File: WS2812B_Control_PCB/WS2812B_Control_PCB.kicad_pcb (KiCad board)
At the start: 2 copper layers, 46.5 x 91.9 mm, 27 parts, among them J1 TB002-500-02BE, J2 TB002-500-02BE, J3 Conn_01x05, J4 S3B-XH-ALFSN, J5 S3B-XH-ALFSN, J6 S3B-XH-ALFSN, J7 S3B-XH-ALFSN, J8 S3B-XH-ALFSN, U1 IRM-20-5, U2 113991254, U3 MC74VHCT50ADTR2G

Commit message: Added 4A current limit to silkscreen
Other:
- board text added: "4A"
- board text added: "IRM-20-5 20W 5V"
- board text removed: "IRM-20-5"
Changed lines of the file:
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@@
 		)
 	)
-	(gr_text "5V"
+	(gr_text "5V\n"
 		(at 17.653 63.627 0)
 		(layer "F.SilkS")
@@
 		)
 	)
+	(gr_text "4A"
+		(at 20.701 63.627 0)
+		(layer "F.SilkS")
+		(effects
+			(font
+				(size 1.5 1.5)
+				(thickness 0.3)
+				(bold yes)
+			)
+			(justify left bottom)
+		)
+	)
 	(gr_text "VOUT"
-		(at 21.082 63.627 0)
+		(at 23.749 63.627 0)
 		(layer "F.SilkS")
 		(effects
@@
 		)
 	)
-	(gr_text "IRM-20-5"
-		(at 61.087 64.897 270)
+	(gr_text "IRM-20-5\n20W 5V"
+		(at 60.96 60.96 270)
 		(layer "B.SilkS")
 		(effects

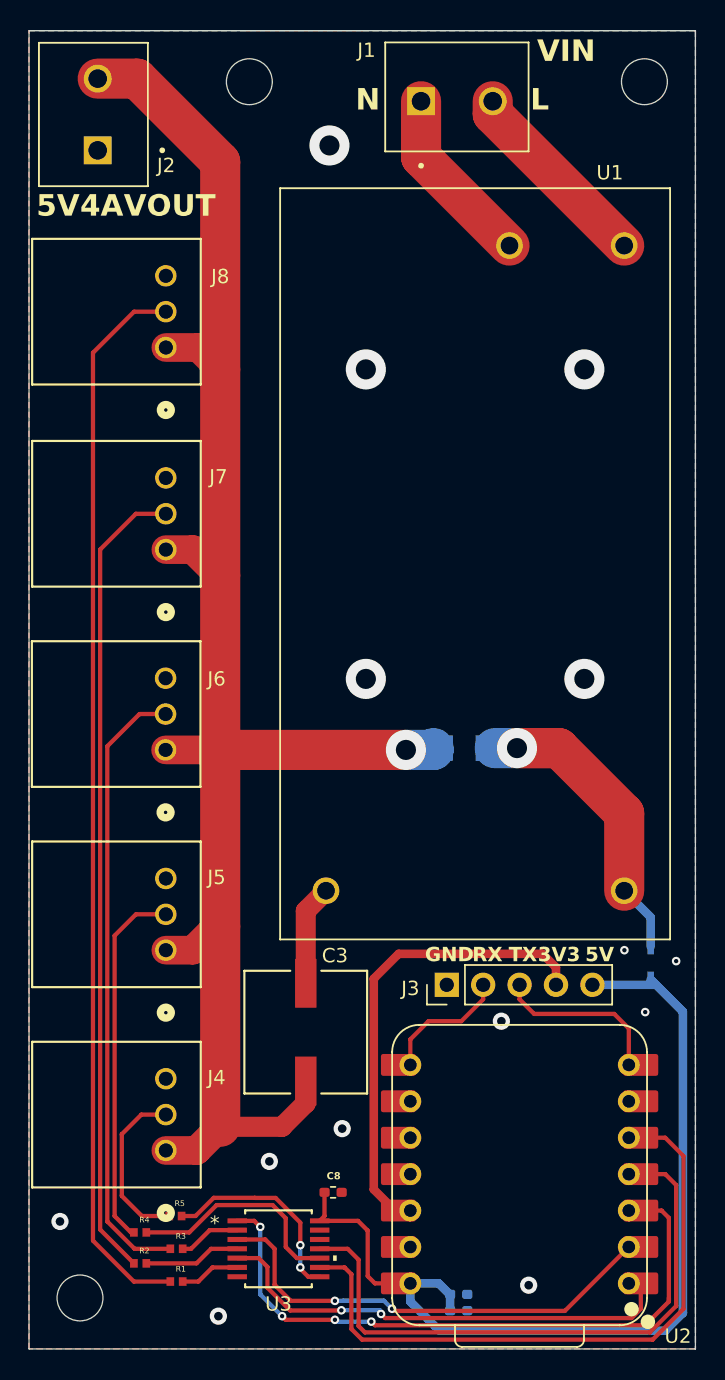
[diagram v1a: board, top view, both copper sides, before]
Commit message: Fixed flaw in v1. Pinout of IRM-20-5 was incorrect. Corrected.
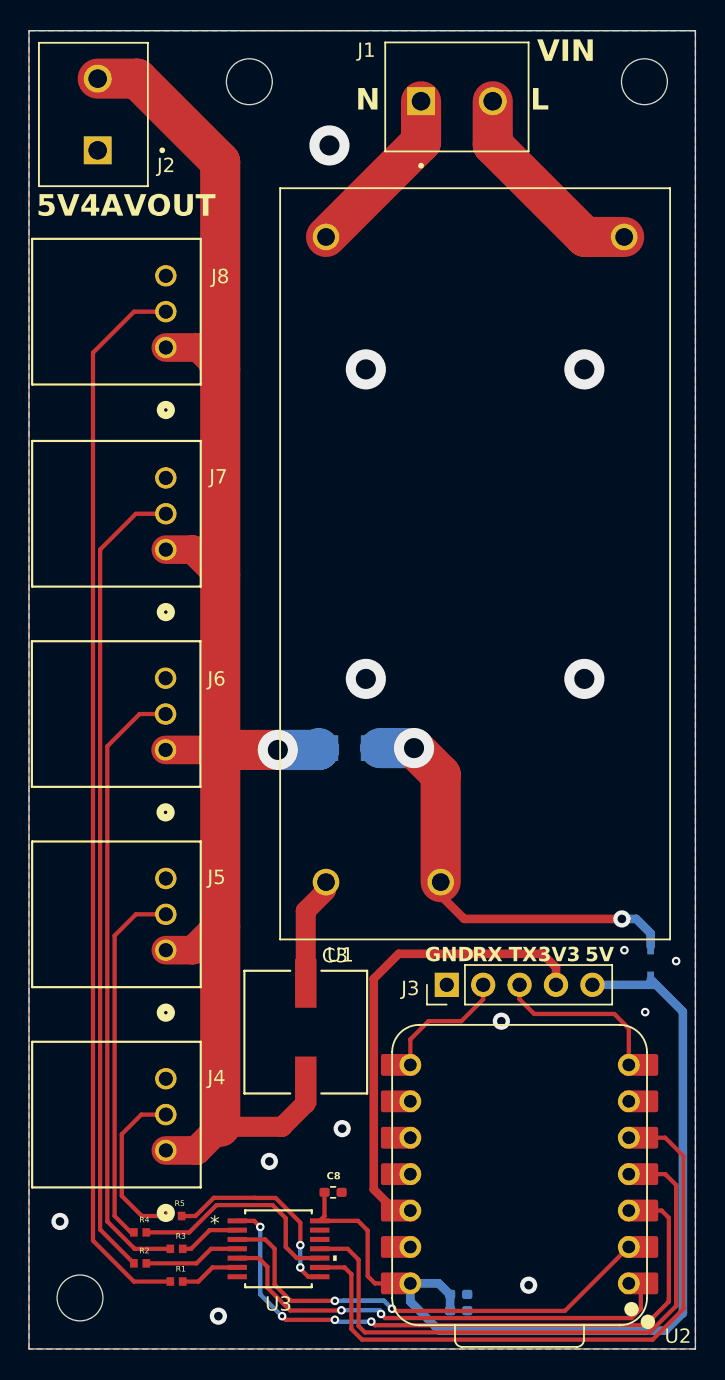
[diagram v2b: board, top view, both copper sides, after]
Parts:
- moved F1 8.00 mm to (39.5, 100.6)
- moved G*** 5.99 mm to (54.5, 106.0)
- moved G*** 1.09 mm to (51.0, 83.0)
- turned U1 to -90 degrees
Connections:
- U1 pad 1: GND -> Net-(U1-AC/L)
- U1 pad 2: VCC -> Net-(U1-AC/N)
- U1 pad 3: Net-(U1-AC/L) -> GND
- U1 pad 4: Net-(U1-AC/N) -> VCC
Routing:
- net Net-(C3-Pad1): track 123.2 -> 115.2 mm
- net VCC: track 23.3 -> 30.1 mm, vias 1 -> 2
- net Net-(U1-AC/L): track 13.9 -> 14.9 mm
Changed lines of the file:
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@@
 	(footprint "WS2812Board:CONV_IRM-20-5"
 		(layer "F.Cu")
-		(at 48.26 87.732 90)
+		(at 48.26 87.732 -90)
 		(property "Reference" "U1"
-			(at 27.28 9.398 180)
+			(at 27.28 9.398 0)
 			(layer "F.SilkS")
 			(effects
@@
 		(duplicate_pad_numbers_are_jumpers no)
 		(fp_line
-			(start 26.2 -13.6)
-			(end 26.2 13.6)
+			(start -26.2 13.6)
+			(end -26.2 -13.6)
 			(stroke
 				(width 0.127)
@@
 		)
 		(fp_line
-			(start -26.2 -13.6)
-			(end 26.2 -13.6)
+			(start 26.2 13.6)
+			(end -26.2 13.6)
 			(stroke
 				(width 0.127)
@@
 		)
 		(fp_line
-			(start 26.2 13.6)
-			(end -26.2 13.6)
+			(start -26.2 -13.6)
+			(end 26.2 -13.6)
 			(stroke
 				(width 0.127)
@@
 		)
 		(fp_line
-			(start -26.2 13.6)
-			(end -26.2 -13.6)
+			(start 26.2 -13.6)
+			(end 26.2 13.6)
 			(stroke
 				(width 0.127)
@@
 		)
 		(fp_line
-			(start 26.45 -13.85)
-			(end 26.45 13.85)
+			(start -26.45 13.85)
+			(end -26.45 -13.85)
 			(stroke
 				(width 0.05)
@@
 		)
 		(fp_line
-			(start -26.45 -13.85)
-			(end 26.45 -13.85)
+			(start 26.45 13.85)
+			(end -26.45 13.85)
 			(stroke
 				(width 0.05)
@@
 		)
 		(fp_line
-			(start 26.45 13.85)
-			(end -26.45 13.85)
+			(start -26.45 -13.85)
+			(end 26.45 -13.85)
 			(stroke
 				(width 0.05)
@@
 		)
 		(fp_line
-			(start -26.45 13.85)
-			(end -26.45 -13.85)
+			(start 26.45 -13.85)
+			(end 26.45 13.85)
 			(stroke
 				(width 0.05)
@@
 		)
 		(fp_line
-			(start 26.2 -13.6)
-			(end 26.2 13.6)
+			(start -26.2 13.6)
+			(end -26.2 -13.6)
 			(stroke
 				(width 0.127)
@@
 		)
 		(fp_line
-			(start -26.2 -13.6)
-			(end 26.2 -13.6)
+			(start 26.2 13.6)
+			(end -26.2 13.6)
 			(stroke
 				(width 0.127)
@@
 		)
 		(fp_line
-			(start 26.2 13.6)
-			(end -26.2 13.6)
+			(start -26.2 -13.6)
+			(end 26.2 -13.6)
 			(stroke
 				(width 0.127)
@@
 		)
 		(fp_line
-			(start -26.2 13.6)
-			(end -26.2 -13.6)
+			(start 26.2 -13.6)
+			(end 26.2 13.6)
 			(stroke
 				(width 0.127)
@@
 		)
 		(pad "1" thru_hole circle
-			(at -22.8 -10.4 90)
+			(at -22.8 -10.4 270)
 			(size 1.86 1.86)
 			(drill 1.24)
 			(layers "*.Cu" "*.Mask")
 			(remove_unused_layers no)
-			(net "GND")
-			(pinfunction "-V_1")
+			(net "Net-(U1-AC{slash}L)")
+			(pinfunction "AC/L_1")
 			(pintype "power_in")
 			(solder_mask_margin 0.102)
 		)
 		(pad "2" thru_hole circle
-			(at -22.8 10.4 90)
+			(at -22.8 10.4 270)
 			(size 1.86 1.86)
 			(drill 1.24)
 			(layers "*.Cu" "*.Mask")
 			(remove_unused_layers no)
-			(net "VCC")
-			(pinfunction "+V_2")
+			(net "Net-(U1-AC{slash}N)")
+			(pinfunction "AC/N_2")
 			(pintype "power_in")
 			(solder_mask_margin 0.102)
 		)
 		(pad "3" thru_hole circle
-			(at 22.2 10.4 90)
+			(at 22.2 10.4 270)
 			(size 1.86 1.86)
 			(drill 1.24)
 			(layers "*.Cu" "*.Mask")
 			(remove_unused_layers no)
-			(net "Net-(U1-AC{slash}L)")
-			(pinfunction "AC/L_3")
+			(net "GND")
+			(pinfunction "-V_3")
 			(pintype "unspecified")
 			(solder_mask_margin 0.102)
 		)
 		(pad "4" thru_hole circle
-			(at 22.2 2.4 90)
+			(at 22.2 2.4 270)
 			(size 1.86 1.86)
 			(drill 1.24)
 			(layers "*.Cu" "*.Mask")
 			(remove_unused_layers no)
-			(net "Net-(U1-AC{slash}N)")
-			(pinfunction "AC/N_4")
+			(net "VCC")
+			(pinfunction "+V_4")
 			(pintype "unspecified")
 			(solder_mask_margin 0.102)
@@
 	(footprint "WS2812Board:viiking"
 		(layer "B.Cu")
-		(at 49.53 109.347 90)
+		(at 54.5 106 90)
 		(property "Reference" "G***"
 			(at 4.572 -0.889 90)
@@
 	(footprint "WS2812Board:moomin"
 		(layer "B.Cu")
-		(at 49.911 83.058 90)
+		(at 51 83 90)
 		(property "Reference" "G***"
 			(at 0 0 90)
@@
 	(footprint "WS2812Board:C1_BEL"
 		(layer "B.Cu")
-		(at 47.498 100.584 180)
+		(at 39.5 100.584 180)
 		(tags "C1T 3.5 ")
 		(property "Reference" "F1"
@@
 			(polygon
 				(pts
-					(xy 48.2346 99.7458) (xy 46.7614 99.7458) (xy 46.7614 101.4222) (xy 48.2346 101.4222)
+					(xy 40.2366 99.7458) (xy 38.7634 99.7458) (xy 38.7634 101.4222) (xy 40.2366 101.4222)
 				)
 			)
@@
 	)
 	(segment
+		(start 34.5 100.711)
+		(end 30.48 100.711)
+		(width 2.8)
+		(layer "F.Cu")
+		(net "Net-(C3-Pad1)")
+	)
+	(segment
 		(start 30.48 113.03)
 		(end 30.48 100.711)
@@
 	)
 	(segment
-		(start 30.48 100.711)
-		(end 43.434 100.711)
-		(width 2.8)
-		(layer "F.Cu")
-		(net "Net-(C3-Pad1)")
-	)
-	(segment
 		(start 26.6879 72.642222)
 		(end 28.954222 72.642222)
@@
 	)
 	(via
-		(at 43.434 100.711)
+		(at 34.5 100.711)
 		(size 2.8)
 		(drill 1.4)
@@
 	)
 	(segment
-		(start 45.3614 100.711)
-		(end 45.3614 100.584)
+		(start 34.5 100.711)
+		(end 37.3634 100.711)
 		(width 2.8)
 		(layer "B.Cu")
@@
 	)
 	(segment
-		(start 43.434 100.711)
-		(end 45.3614 100.711)
+		(start 37.3634 100.711)
+		(end 37.3634 100.584)
 		(width 2.8)
 		(layer "B.Cu")
@@
 	)
 	(segment
-		(start 58.66 105.142)
-		(end 58.66 110.532)
-		(width 2.8)
+		(start 58.5 112.5)
+		(end 47.5 112.5)
+		(width 0.6)
 		(layer "F.Cu")
 		(net "VCC")
 	)
 	(segment
-		(start 51.181 100.584)
-		(end 54.102 100.584)
-		(width 2.8)
+		(start 45.86 110.86)
+		(end 45.86 109.932)
+		(width 0.6)
 		(layer "F.Cu")
 		(net "VCC")
 	)
 	(segment
-		(start 51.181 100.584)
-		(end 53.467 100.584)
+		(start 47.5 112.5)
+		(end 45.86 110.86)
+		(width 0.6)
+		(layer "F.Cu")
+		(net "VCC")
+	)
+	(segment
+		(start 45.86 102.444)
+		(end 44 100.584)
 		(width 2.8)
 		(layer "F.Cu")
@@
 	)
 	(segment
-		(start 54.102 100.584)
-		(end 58.66 105.142)
+		(start 45.86 109.932)
+		(end 45.86 102.444)
 		(width 2.8)
 		(layer "F.Cu")
@@
 	)
 	(via
-		(at 51.181 100.584)
+		(at 58.5 112.5)
+		(size 1.2)
+		(drill 0.6)
+		(layers "F.Cu" "B.Cu")
+		(net "VCC")
+	)
+	(via
+		(at 44 100.584)
 		(size 2.8)
 		(drill 1.4)
@@
 	)
 	(segment
-		(start 60.506 114.42)
-		(end 60.506 112.378)
+		(start 59.5 112.5)
+		(end 58.5 112.5)
 		(width 0.6)
 		(layer "B.Cu")
@@
 	)
 	(segment
-		(start 58.66 110.532)
-		(end 58.618 110.49)
-		(width 0.6)
+		(start 44 100.584)
+		(end 41.6366 100.584)
+		(width 2.8)
 		(layer "B.Cu")
 		(net "VCC")
 	)
 	(segment
-		(start 60.506 112.378)
-		(end 58.66 110.532)
+		(start 60.506 113.506)
+		(end 59.5 112.5)
 		(width 0.6)
 		(layer "B.Cu")
@@
 	)
 	(segment
-		(start 51.181 100.584)
-		(end 49.6346 100.584)
-		(width 2.8)
+		(start 60.506 114.42)
+		(end 60.506 113.506)
+		(width 0.6)
 		(layer "B.Cu")
 		(net "VCC")
 	)
 	(segment
-		(start 49.49 56.362)
-		(end 58.66 65.532)
+		(start 49.49 55.4635)
+		(end 49.49 58.49)
+		(width 2.8)
+		(layer "F.Cu")
+		(net "Net-(U1-AC{slash}L)")
+	)
+	(segment
+		(start 55.932 64.932)
+		(end 58.66 64.932)
 		(width 2.8)
 		(layer "F.Cu")
@@
 	)
 	(segment
-		(start 49.49 55.4635)
-		(end 49.49 56.362)
+		(start 49.49 58.49)
+		(end 55.932 64.932)
 		(width 2.8)
 		(layer "F.Cu")
@@
 	)
 	(segment
-		(start 44.49 55.4635)
-		(end 44.49 59.362)
+		(start 37.86 64.932)
+		(end 44.49 58.302)
 		(width 2.8)
 		(layer "F.Cu")
@@
 	)
 	(segment
-		(start 44.49 59.362)
-		(end 50.66 65.532)
+		(start 44.49 58.302)
+		(end 44.49 55.4635)
 		(width 2.8)
 		(layer "F.Cu")
